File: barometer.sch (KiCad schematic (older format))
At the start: 4 parts, among them U5 MPL3115A2

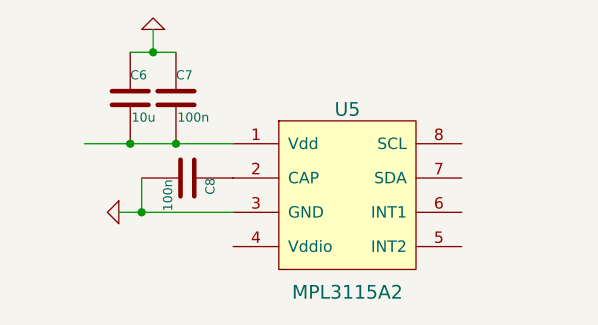
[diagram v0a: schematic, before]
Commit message: Add gps
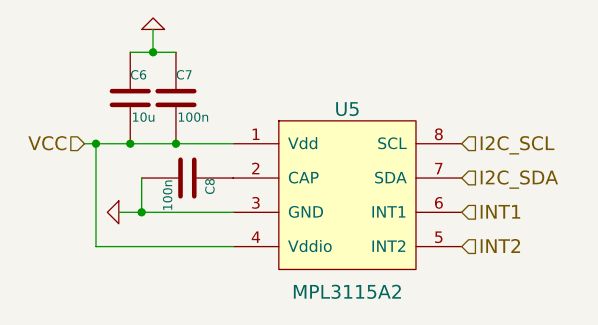
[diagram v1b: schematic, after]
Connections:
- net labels added: I2C_SCL, I2C_SDA, INT1, INT2, VCC
- wire segments 5 -> 7
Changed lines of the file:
@@
 $Descr A4 11693 8268
 encoding utf-8
-Sheet 5 10
+Sheet 5 11
 Title ""
 Date ""
@@
 $EndComp
 $Comp
-L GND #PWR8
+L GND #PWR13
 U 1 1 54462E61
 P 5100 4600
-F 0 "#PWR8" H 5100 4600 30  0001 C CNN
+F 0 "#PWR13" H 5100 4600 30  0001 C CNN
 F 1 "GND" H 5100 4530 30  0001 C CNN
 F 2 "" H 5100 4600 60  0000 C CNN
@@
 Connection ~ 5150 4300
 $Comp
-L GND #PWR9
+L GND #PWR14
 U 1 1 54462E79
 P 5250 3800
-F 0 "#PWR9" H 5250 3800 30  0001 C CNN
+F 0 "#PWR14" H 5250 3800 30  0001 C CNN
 F 1 "GND" H 5250 3730 30  0001 C CNN
 F 2 "" H 5250 3800 60  0000 C CNN
@@
 	5200 4450 5200 4600
 Connection ~ 5200 4600
+Text HLabel 6600 4300 2    60   Input ~ 0
+I2C_SCL
+Text HLabel 6600 4450 2    60   Input ~ 0
+I2C_SDA
+Text HLabel 6600 4600 2    60   Input ~ 0
+INT1
+Text HLabel 6600 4750 2    60   Input ~ 0
+INT2
+Text HLabel 4950 4300 0    60   Input ~ 0
+VCC
+Wire Wire Line
+	5600 4750 5000 4750
+Wire Wire Line
+	5000 4750 5000 4300
+Connection ~ 5000 4300
 $EndSCHEMATC

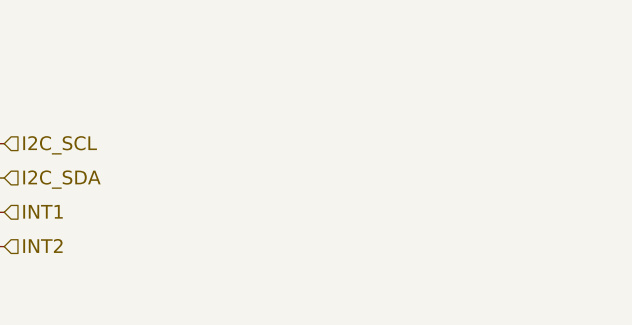
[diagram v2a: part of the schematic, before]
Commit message: More connections
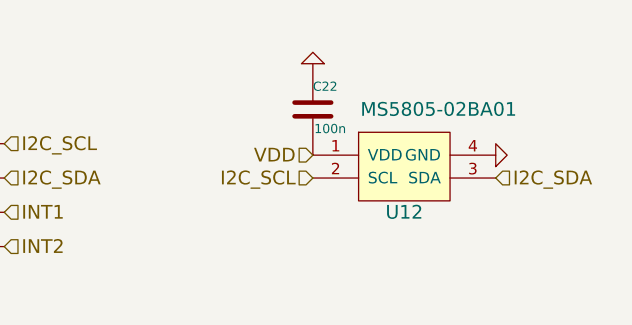
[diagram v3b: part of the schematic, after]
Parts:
- added C22: 100n, buq2:SM0603, symbol C
- added U12: MS5805-02BA01, buq2:MS5805-02BA01, symbol MS5805-02BA01
- C6: footprint (none) -> buq2:SM1206
- C7, C8: footprint (none) -> buq2:SM0603
- U5: footprint (none) -> buq2:8-TLGA
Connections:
- net GND: now also C22.1, U12.4 (GND)
- net I2C_SCL: now also U12.2 (SCL)
- net I2C_SDA: now also U12.3 (SDA)
- new net VDD: C22.2, U12.1 (VDD)
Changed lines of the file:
@@
 F 0 "U5" H 6100 4950 60  0000 C CNN
 F 1 "MPL3115A2" H 6100 4150 60  0000 C CNN
-F 2 "" H 6100 4550 60  0001 C CNN
+F 2 "buq2:8-TLGA" H 6100 4550 60  0001 C CNN
 F 3 "" H 6100 4550 60  0000 C CNN
 	1    6100 4550
@@
 $EndComp
 $Comp
-L GND #PWR13
+L GND #PWR013
 U 1 1 54462E61
 P 5100 4600
-F 0 "#PWR13" H 5100 4600 30  0001 C CNN
+F 0 "#PWR013" H 5100 4600 30  0001 C CNN
 F 1 "GND" H 5100 4530 30  0001 C CNN
 F 2 "" H 5100 4600 60  0000 C CNN
@@
 F 0 "C7" H 5350 4200 40  0000 L CNN
 F 1 "100n" H 5356 4015 40  0000 L CNN
-F 2 "" H 5388 3950 30  0001 C CNN
+F 2 "buq2:SM0603" H 5388 3950 30  0001 C CNN
 F 3 "" H 5350 4100 60  0000 C CNN
 	1    5350 4100
@@
 F 0 "C6" H 5150 4200 40  0000 L CNN
 F 1 "10u" H 5156 4015 40  0000 L CNN
-F 2 "" H 5188 3950 30  0001 C CNN
+F 2 "buq2:SM1206" H 5188 3950 30  0001 C CNN
 F 3 "" H 5150 4100 60  0000 C CNN
 	1    5150 4100
@@
 Connection ~ 5150 4300
 $Comp
-L GND #PWR14
+L GND #PWR014
 U 1 1 54462E79
 P 5250 3800
-F 0 "#PWR14" H 5250 3800 30  0001 C CNN
+F 0 "#PWR014" H 5250 3800 30  0001 C CNN
 F 1 "GND" H 5250 3730 30  0001 C CNN
 F 2 "" H 5250 3800 60  0000 C CNN
@@
 F 0 "C8" H 5400 4550 40  0000 L CNN
 F 1 "100n" H 5406 4365 40  0000 L CNN
-F 2 "" H 5438 4300 30  0001 C CNN
+F 2 "buq2:SM0603" H 5438 4300 30  0001 C CNN
 F 3 "" H 5400 4450 60  0000 C CNN
 	1    5400 4450
@@
 	5000 4750 5000 4300
 Connection ~ 5000 4300
+$Comp
+L MS5805-02BA01 U12
+U 1 1 54633C77
+P 8350 4400
+F 0 "U12" H 8350 4200 60  0000 C CNN
+F 1 "MS5805-02BA01" H 8500 4650 60  0000 C CNN
+F 2 "buq2:MS5805-02BA01" H 8350 4300 60  0001 C CNN
+F 3 "" H 8350 4300 60  0000 C CNN
+	1    8350 4400
+	1    0    0    -1
+$EndComp
+Text HLabel 7950 4450 0    60   Input ~ 0
+I2C_SCL
+Text HLabel 8750 4450 2    60   Input ~ 0
+I2C_SDA
+$Comp
+L GND #PWR015
+U 1 1 54633D5C
+P 8750 4350
+F 0 "#PWR015" H 8750 4350 30  0001 C CNN
+F 1 "GND" H 8750 4280 30  0001 C CNN
+F 2 "" H 8750 4350 60  0000 C CNN
+F 3 "" H 8750 4350 60  0000 C CNN
+	1    8750 4350
+	0    -1   -1   0
+$EndComp
+$Comp
+L C C22
+U 1 1 54633DDE
+P 7950 4150
+F 0 "C22" H 7950 4250 40  0000 L CNN
+F 1 "100n" H 7956 4065 40  0000 L CNN
+F 2 "buq2:SM0603" H 7988 4000 30  0001 C CNN
+F 3 "" H 7950 4150 60  0000 C CNN
+	1    7950 4150
+	1    0    0    -1
+$EndComp
+$Comp
+L GND #PWR016
+U 1 1 54633E1B
+P 7950 3950
+F 0 "#PWR016" H 7950 3950 30  0001 C CNN
+F 1 "GND" H 7950 3880 30  0001 C CNN
+F 2 "" H 7950 3950 60  0000 C CNN
+F 3 "" H 7950 3950 60  0000 C CNN
+	1    7950 3950
+	-1   0    0    1
+$EndComp
+Text HLabel 7950 4350 0    60   Input ~ 0
+VDD
 $EndSCHEMATC

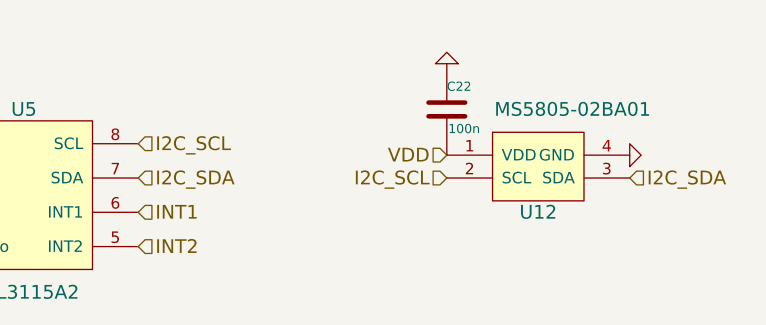
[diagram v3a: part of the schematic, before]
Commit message: Add flash and ram. Some connections and DRC cleaning
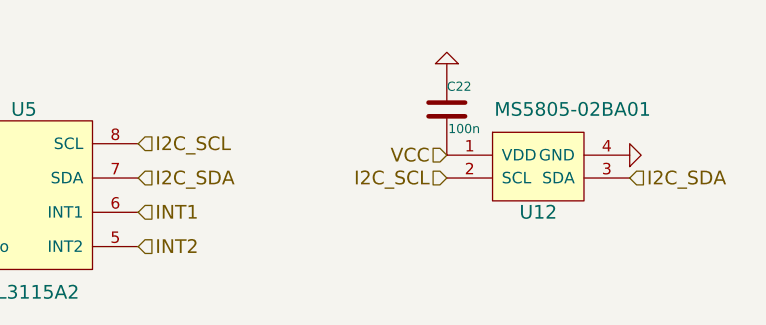
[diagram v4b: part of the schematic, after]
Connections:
- net VDD is gone; now on net VCC: C22.2, U12.1 (VDD)
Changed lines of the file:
@@
 $Descr A4 11693 8268
 encoding utf-8
-Sheet 5 12
+Sheet 5 13
 Title ""
 Date ""
@@
 $EndComp
 $Comp
-L GND #PWR013
+L GND #PWR014
 U 1 1 54462E61
 P 5100 4600
-F 0 "#PWR013" H 5100 4600 30  0001 C CNN
+F 0 "#PWR014" H 5100 4600 30  0001 C CNN
 F 1 "GND" H 5100 4530 30  0001 C CNN
 F 2 "" H 5100 4600 60  0000 C CNN
@@
 Connection ~ 5150 4300
 $Comp
-L GND #PWR014
+L GND #PWR015
 U 1 1 54462E79
 P 5250 3800
-F 0 "#PWR014" H 5250 3800 30  0001 C CNN
+F 0 "#PWR015" H 5250 3800 30  0001 C CNN
 F 1 "GND" H 5250 3730 30  0001 C CNN
 F 2 "" H 5250 3800 60  0000 C CNN
@@
 I2C_SDA
 $Comp
-L GND #PWR015
+L GND #PWR016
 U 1 1 54633D5C
 P 8750 4350
-F 0 "#PWR015" H 8750 4350 30  0001 C CNN
+F 0 "#PWR016" H 8750 4350 30  0001 C CNN
 F 1 "GND" H 8750 4280 30  0001 C CNN
 F 2 "" H 8750 4350 60  0000 C CNN
@@
 $EndComp
 $Comp
-L GND #PWR016
+L GND #PWR017
 U 1 1 54633E1B
 P 7950 3950
-F 0 "#PWR016" H 7950 3950 30  0001 C CNN
+F 0 "#PWR017" H 7950 3950 30  0001 C CNN
 F 1 "GND" H 7950 3880 30  0001 C CNN
 F 2 "" H 7950 3950 60  0000 C CNN
@@
 $EndComp
 Text HLabel 7950 4350 0    60   Input ~ 0
-VDD
+VCC
 $EndSCHEMATC

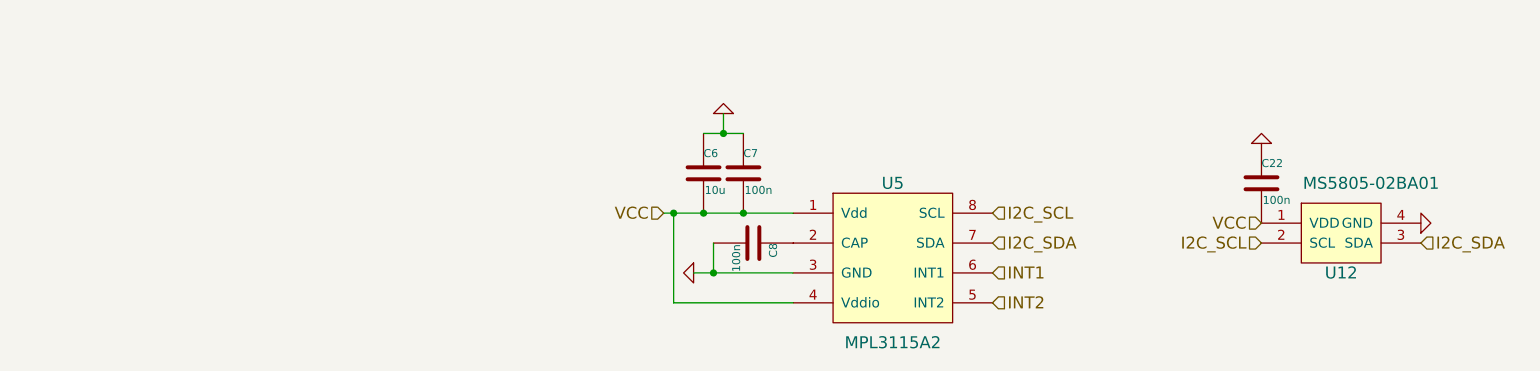
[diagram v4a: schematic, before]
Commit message: Add buttons. Fix DRC. Add antenna
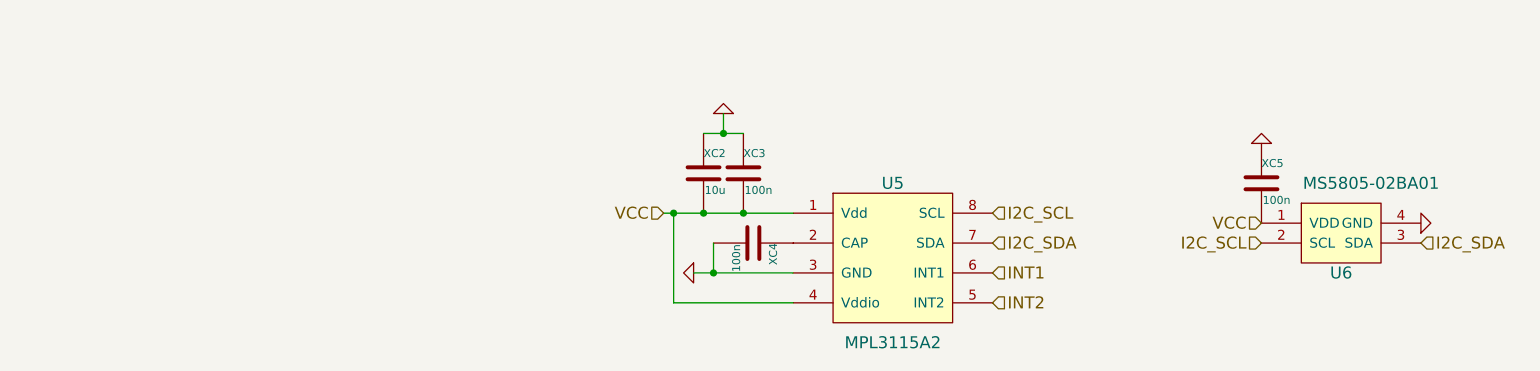
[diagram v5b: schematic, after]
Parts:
- renumbered U12 to U6, C6 to XC2, C7 to XC3, C8 to XC4, C22 to XC5
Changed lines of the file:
@@
 $Descr A4 11693 8268
 encoding utf-8
-Sheet 5 13
+Sheet 5 14
 Title ""
 Date ""
@@
 $EndComp
 $Comp
-L GND #PWR014
+L GND #PWR015
 U 1 1 54462E61
 P 5100 4600
-F 0 "#PWR014" H 5100 4600 30  0001 C CNN
+F 0 "#PWR015" H 5100 4600 30  0001 C CNN
 F 1 "GND" H 5100 4530 30  0001 C CNN
 F 2 "" H 5100 4600 60  0000 C CNN
@@
 	5100 4600 5600 4600
 $Comp
-L C C7
+L C XC3
 U 1 1 54462E68
 P 5350 4100
-F 0 "C7" H 5350 4200 40  0000 L CNN
+F 0 "XC3" H 5350 4200 40  0000 L CNN
 F 1 "100n" H 5356 4015 40  0000 L CNN
 F 2 "buq2:SM0603" H 5388 3950 30  0001 C CNN
@@
 $EndComp
 $Comp
-L C C6
+L C XC2
 U 1 1 54462E6F
 P 5150 4100
-F 0 "C6" H 5150 4200 40  0000 L CNN
+F 0 "XC2" H 5150 4200 40  0000 L CNN
 F 1 "10u" H 5156 4015 40  0000 L CNN
 F 2 "buq2:SM1206" H 5188 3950 30  0001 C CNN
@@
 Connection ~ 5150 4300
 $Comp
-L GND #PWR015
+L GND #PWR016
 U 1 1 54462E79
 P 5250 3800
-F 0 "#PWR015" H 5250 3800 30  0001 C CNN
+F 0 "#PWR016" H 5250 3800 30  0001 C CNN
 F 1 "GND" H 5250 3730 30  0001 C CNN
 F 2 "" H 5250 3800 60  0000 C CNN
@@
 Connection ~ 5250 3900
 $Comp
-L C C8
+L C XC4
 U 1 1 54462E82
 P 5400 4450
-F 0 "C8" H 5400 4550 40  0000 L CNN
+F 0 "XC4" H 5400 4550 40  0000 L CNN
 F 1 "100n" H 5406 4365 40  0000 L CNN
 F 2 "buq2:SM0603" H 5438 4300 30  0001 C CNN
@@
 Connection ~ 5000 4300
 $Comp
-L MS5805-02BA01 U12
+L MS5805-02BA01 U6
 U 1 1 54633C77
 P 8350 4400
-F 0 "U12" H 8350 4200 60  0000 C CNN
+F 0 "U6" H 8350 4200 60  0000 C CNN
 F 1 "MS5805-02BA01" H 8500 4650 60  0000 C CNN
 F 2 "buq2:MS5805-02BA01" H 8350 4300 60  0001 C CNN
@@
 I2C_SDA
 $Comp
-L GND #PWR016
+L GND #PWR017
 U 1 1 54633D5C
 P 8750 4350
-F 0 "#PWR016" H 8750 4350 30  0001 C CNN
+F 0 "#PWR017" H 8750 4350 30  0001 C CNN
 F 1 "GND" H 8750 4280 30  0001 C CNN
 F 2 "" H 8750 4350 60  0000 C CNN
@@
 $EndComp
 $Comp
-L C C22
+L C XC5
 U 1 1 54633DDE
 P 7950 4150
-F 0 "C22" H 7950 4250 40  0000 L CNN
+F 0 "XC5" H 7950 4250 40  0000 L CNN
 F 1 "100n" H 7956 4065 40  0000 L CNN
 F 2 "buq2:SM0603" H 7988 4000 30  0001 C CNN
@@
 $EndComp
 $Comp
-L GND #PWR017
+L GND #PWR018
 U 1 1 54633E1B
 P 7950 3950
-F 0 "#PWR017" H 7950 3950 30  0001 C CNN
+F 0 "#PWR018" H 7950 3950 30  0001 C CNN
 F 1 "GND" H 7950 3880 30  0001 C CNN
 F 2 "" H 7950 3950 60  0000 C CNN

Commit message: Start first layout test
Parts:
- XC2: footprint buq2:SM1206 -> buq2:SM0805
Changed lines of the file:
@@
 F 0 "XC2" H 5150 4200 40  0000 L CNN
 F 1 "10u" H 5156 4015 40  0000 L CNN
-F 2 "buq2:SM1206" H 5188 3950 30  0001 C CNN
+F 2 "buq2:SM0805" H 5188 3950 30  0001 C CNN
 F 3 "" H 5150 4100 60  0000 C CNN
 	1    5150 4100

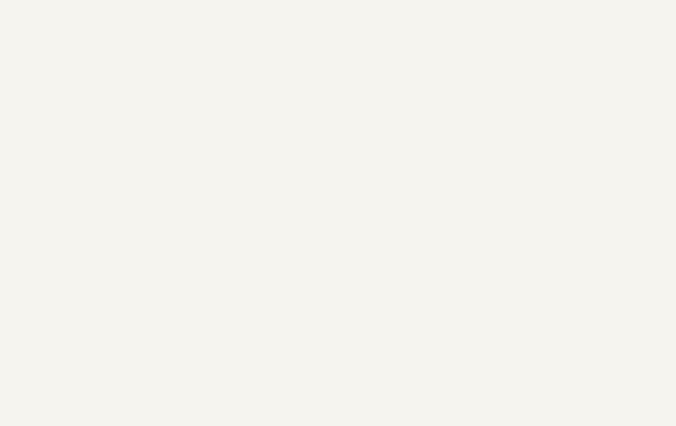
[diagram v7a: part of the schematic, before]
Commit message: Add new barometer
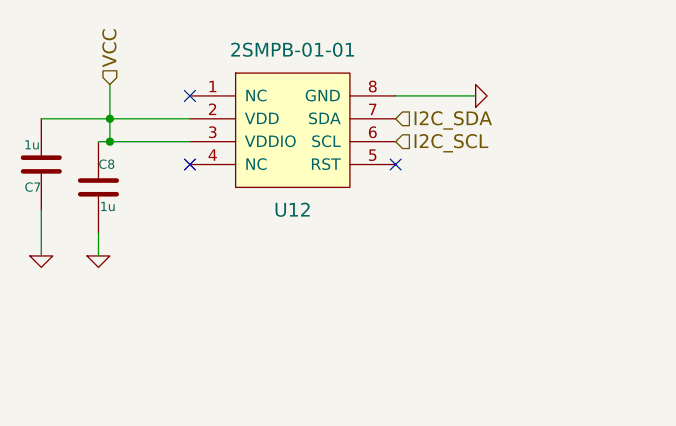
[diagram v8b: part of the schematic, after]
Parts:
- added C7, C8: 1u, symbol C
- added U12: 2SMPB-01-01, symbol 2SMPB-01-01
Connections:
- net GND: now also C7.1, C8.2, U12.8 (GND)
- net I2C_SCL: now also U12.6 (SCL)
- net I2C_SDA: now also U12.7 (SDA)
- net VCC: now also C7.2, C8.1, U12.2 (VDD), U12.3 (VDDIO)
- no-connect marks 0 -> 3
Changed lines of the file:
@@
 $EndComp
 $Comp
-L GND #PWR013
+L GND #PWR14
 U 1 1 54462E61
 P 5100 4600
-F 0 "#PWR013" H 5100 4600 30  0001 C CNN
+F 0 "#PWR14" H 5100 4600 30  0001 C CNN
 F 1 "GND" H 5100 4530 30  0001 C CNN
 F 2 "" H 5100 4600 60  0000 C CNN
@@
 Connection ~ 5150 4300
 $Comp
-L GND #PWR014
+L GND #PWR15
 U 1 1 54462E79
 P 5250 3800
-F 0 "#PWR014" H 5250 3800 30  0001 C CNN
+F 0 "#PWR15" H 5250 3800 30  0001 C CNN
 F 1 "GND" H 5250 3730 30  0001 C CNN
 F 2 "" H 5250 3800 60  0000 C CNN
@@
 I2C_SDA
 $Comp
-L GND #PWR015
+L GND #PWR17
 U 1 1 54633D5C
 P 8750 4350
-F 0 "#PWR015" H 8750 4350 30  0001 C CNN
+F 0 "#PWR17" H 8750 4350 30  0001 C CNN
 F 1 "GND" H 8750 4280 30  0001 C CNN
 F 2 "" H 8750 4350 60  0000 C CNN
@@
 $EndComp
 $Comp
-L GND #PWR016
+L GND #PWR16
 U 1 1 54633E1B
 P 7950 3950
-F 0 "#PWR016" H 7950 3950 30  0001 C CNN
+F 0 "#PWR16" H 7950 3950 30  0001 C CNN
 F 1 "GND" H 7950 3880 30  0001 C CNN
 F 2 "" H 7950 3950 60  0000 C CNN
@@
 Text HLabel 7950 4350 0    60   Input ~ 0
 VCC
+$Comp
+L 2SMPB-01-01 U12
+U 1 1 54C7F8FE
+P 2900 3850
+F 0 "U12" H 2900 3550 60  0000 C CNN
+F 1 "2SMPB-01-01" H 2900 4250 60  0000 C CNN
+F 2 "" H 2800 3850 60  0000 C CNN
+F 3 "" H 2800 3850 60  0000 C CNN
+	1    2900 3850
+	1    0    0    -1
+$EndComp
+$Comp
+L GND #PWR13
+U 1 1 54C7F9CA
+P 3700 3650
+F 0 "#PWR13" H 3700 3650 30  0001 C CNN
+F 1 "GND" H 3700 3580 30  0001 C CNN
+F 2 "" H 3700 3650 60  0000 C CNN
+F 3 "" H 3700 3650 60  0000 C CNN
+	1    3700 3650
+	0    -1   -1   0
+$EndComp
+Wire Wire Line
+	3700 3650 3350 3650
+Text HLabel 3350 3750 2    60   Input ~ 0
+I2C_SDA
+Text HLabel 3350 3850 2    60   Input ~ 0
+I2C_SCL
+$Comp
+L C C7
+U 1 1 54C7FA3D
+P 1800 3950
+F 0 "C7" H 1800 4050 40  0000 L CNN
+F 1 "1u" H 1806 3865 40  0000 L CNN
+F 2 "" H 1838 3800 30  0000 C CNN
+F 3 "" H 1800 3950 60  0000 C CNN
+	1    1800 3950
+	-1   0    0    1
+$EndComp
+$Comp
+L C C8
+U 1 1 54C7FAA3
+P 2050 4050
+F 0 "C8" H 2050 4150 40  0000 L CNN
+F 1 "1u" H 2056 3965 40  0000 L CNN
+F 2 "" H 2088 3900 30  0000 C CNN
+F 3 "" H 2050 4050 60  0000 C CNN
+	1    2050 4050
+	1    0    0    -1
+$EndComp
+$Comp
+L GND #PWR12
+U 1 1 54C7FACF
+P 2050 4350
+F 0 "#PWR12" H 2050 4350 30  0001 C CNN
+F 1 "GND" H 2050 4280 30  0001 C CNN
+F 2 "" H 2050 4350 60  0000 C CNN
+F 3 "" H 2050 4350 60  0000 C CNN
+	1    2050 4350
+	1    0    0    -1
+$EndComp
+$Comp
+L GND #PWR11
+U 1 1 54C7FAF3
+P 1800 4350
+F 0 "#PWR11" H 1800 4350 30  0001 C CNN
+F 1 "GND" H 1800 4280 30  0001 C CNN
+F 2 "" H 1800 4350 60  0000 C CNN
+F 3 "" H 1800 4350 60  0000 C CNN
+	1    1800 4350
+	1    0    0    -1
+$EndComp
+Wire Wire Line
+	1800 4350 1800 4150
+Wire Wire Line
+	2050 4350 2050 4250
+Wire Wire Line
+	2450 3850 2050 3850
+Wire Wire Line
+	1800 3750 2450 3750
+NoConn ~ 2450 3650
+NoConn ~ 2450 3950
+NoConn ~ 3350 3950
+Text HLabel 2100 3600 1    60   Input ~ 0
+VCC
+Wire Wire Line
+	2100 3600 2100 3850
+Connection ~ 2100 3750
+Connection ~ 2100 3850
 $EndSCHEMATC
